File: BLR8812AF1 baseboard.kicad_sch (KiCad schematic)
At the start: 28 parts, among them U1 MP2307DN, U2 USBLC6-2SC6, U3 BL-R8812AF1, X1 TYPE-C-31-M-12

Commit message: Working on board
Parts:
- removed MH (x3): MountingHole, symbol Mechanical:MountingHole
- added MH2, MH3, MH4: MountingHole, MountingHole:MountingHole_2.2mm_M2, symbol Mechanical:MountingHole
- added X2, X5: ~, ULF:TH_1.7_1.7_1, symbol Ulf:TH_1_Pin
- added X3, X4, X6: ~, ULF:TH_1_1_0.65, symbol Ulf:TH_1_Pin
- C1, C2: value 10u -> 22u
- L1: footprint PCM_Inductor_SMD_AKL:L_7.3x7.3_H4.5 -> Inductor_SMD:L_SXN_SMDRI62
- MH1: renamed from MH; footprint (none) -> MountingHole:MountingHole_2.2mm_M2
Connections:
- net GND: now also X5.1 (Pin_1), X6.1 (Pin_1)
- net VBUS: now also X2.1 (Pin_1)
- net DP: now reaches U2.1 (I/O1), X1.A6 (DP1), X1.B6 (DP2)
- net DP: now also X3.1 (Pin_1)
- net DN: now reaches U2.3 (I/O2), X1.A7 (DN1), X1.B7 (DN2)
- net DN: now also X4.1 (Pin_1)
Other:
- moved on the sheet: C8, D1

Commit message: Completed placing
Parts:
- added D2: DNP, LED_SMD:LED_0603_1608Metric, symbol Device:LED
- added R10: DNP, Resistor_SMD:R_0402_1005Metric, symbol Device:R
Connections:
- net 3V3: now also R10.2
- net GND: now also D2.1 (K)
- net D1_P: now reaches R4.1, U2.6 (I/O1)
- net D2_P: now reaches R4.2, U3.4 (DP)
- net D2_N: now reaches R5.2, U3.3 (DN)
- net D1_N: now reaches R5.1, U2.4 (I/O2)
- new net: D2.2 (A), R10.1
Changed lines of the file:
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@@
 	)
 	(junction
+		(at 142.24 153.67)
+		(diameter 0)
+		(color 0 0 0 0)
+	)
+	(junction
 		(at 46.99 88.9)
 		(diameter 0)
@@
 	(wire
 		(pts
+			(xy 152.4 148.59) (xy 152.4 153.67)
+		)
+		(stroke
+			(width 0)
+			(type default)
+		)
+	)
+	(wire
+		(pts
 			(xy 132.08 69.85) (xy 129.54 69.85)
 		)
@@
 	(wire
 		(pts
+			(xy 152.4 132.08) (xy 152.4 127)
+		)
+		(stroke
+			(width 0)
+			(type default)
+		)
+	)
+	(wire
+		(pts
 			(xy 200.66 53.34) (xy 200.66 52.07)
 		)
@@
 	(wire
 		(pts
+			(xy 152.4 127) (xy 142.24 127)
+		)
+		(stroke
+			(width 0)
+			(type default)
+		)
+	)
+	(wire
+		(pts
 			(xy 142.24 124.46) (xy 142.24 127)
 		)
@@
 	(wire
 		(pts
+			(xy 152.4 139.7) (xy 152.4 140.97)
+		)
+		(stroke
+			(width 0)
+			(type default)
+		)
+	)
+	(wire
+		(pts
 			(xy 62.23 40.64) (xy 68.58 40.64)
 		)
@@
 	(wire
 		(pts
+			(xy 152.4 153.67) (xy 142.24 153.67)
+		)
+		(stroke
+			(width 0)
+			(type default)
+		)
+	)
+	(wire
+		(pts
 			(xy 43.18 143.51) (xy 49.53 143.51)
 		)
@@
 		)
 	)
+	(label "D2_P"
+		(at 106.68 38.1 0)
+		(fields_autoplaced yes)
+		(effects
+			(font
+				(size 1.27 1.27)
+			)
+			(justify left bottom)
+		)
+	)
+	(label "D2_N"
+		(at 106.68 40.64 0)
+		(fields_autoplaced yes)
+		(effects
+			(font
+				(size 1.27 1.27)
+			)
+			(justify left bottom)
+		)
+	)
 	(label "DP"
 		(at 177.8 57.15 180)
@@
 		)
 	)
+	(label "D1_P"
+		(at 88.9 38.1 0)
+		(fields_autoplaced yes)
+		(effects
+			(font
+				(size 1.27 1.27)
+			)
+			(justify left bottom)
+		)
+	)
 	(label "DN"
 		(at 72.39 40.64 0)
@@
 		)
 	)
+	(label "D1_N"
+		(at 88.9 40.64 0)
+		(fields_autoplaced yes)
+		(effects
+			(font
+				(size 1.27 1.27)
+			)
+			(justify left bottom)
+		)
+	)
 	(symbol
 		(lib_id "Mechanical:MountingHole")
@@
 	)
 	(symbol
+		(lib_id "Device:LED")
+		(at 152.4 144.78 90)
+		(unit 1)
+		(exclude_from_sim no)
+		(in_bom yes)
+		(on_board yes)
+		(dnp no)
+		(property "Reference" "D2"
+			(at 155.194 144.78 0)
+			(effects
+				(font
+					(size 1.27 1.27)
+				)
+			)
+		)
+		(property "Value" "DNP"
+			(at 149.86 144.78 0)
+			(effects
+				(font
+					(size 1.27 1.27)
+				)
+			)
+		)
+		(property "Footprint" "LED_SMD:LED_0603_1608Metric"
+			(at 152.4 144.78 0)
+			(effects
+				(font
+					(size 1.27 1.27)
+				)
+				(hide yes)
+			)
+		)
+		(property "Datasheet" "~"
+			(at 152.4 144.78 0)
+			(effects
+				(font
+					(size 1.27 1.27)
+				)
+				(hide yes)
+			)
+		)
+		(property "Description" "Light emitting diode"
+			(at 152.4 144.78 0)
+			(effects
+				(font
+					(size 1.27 1.27)
+				)
+				(hide yes)
+			)
+		)
+		(pin "2"
+		)
+		(pin "1"
+		)
+		(instances
+			(project "BLR8812AF1 baseboard"
+				(path "/eaa389b1-c28c-408b-8713-22e94bf6c980"
+					(reference "D2")
+					(unit 1)
+				)
+			)
+		)
+	)
+	(symbol
 		(lib_id "Device:R")
 		(at 99.06 148.59 180)
@@
 					(unit 1)
 				)
+			)
+		)
+	)
+	(symbol
+		(lib_id "Device:R")
+		(at 152.4 135.89 180)
+		(unit 1)
+		(exclude_from_sim no)
+		(in_bom yes)
+		(on_board yes)
+		(dnp no)
+		(property "Reference" "R10"
+			(at 150.114 135.89 90)
+			(effects
+				(font
+					(size 1.27 1.27)
+				)
+			)
+		)
+		(property "Value" "DNP"
+			(at 154.94 135.89 90)
+			(effects
+				(font
+					(size 1.27 1.27)
+				)
+			)
+		)
+		(property "Footprint" "Resistor_SMD:R_0402_1005Metric"
+			(at 154.178 135.89 90)
+			(effects
+				(font
+					(size 1.27 1.27)
+				)
+				(hide yes)
+			)
+		)
+		(property "Datasheet" "~"
+			(at 152.4 135.89 0)
+			(effects
+				(font
+					(size 1.27 1.27)
+				)
+				(hide yes)
+			)
+		)
+		(property "Description" "Resistor"
+			(at 152.4 135.89 0)
+			(effects
+				(font
+					(size 1.27 1.27)
+				)
+				(hide yes)
+			)
+		)
+		(pin "1"
+		)
+		(pin "2"
+		)
+		(instances
+			(project "BLR8812AF1 baseboard"
+				(path "/eaa389b1-c28c-408b-8713-22e94bf6c980"
+					(reference "R10")
+					(unit 1)
+				)

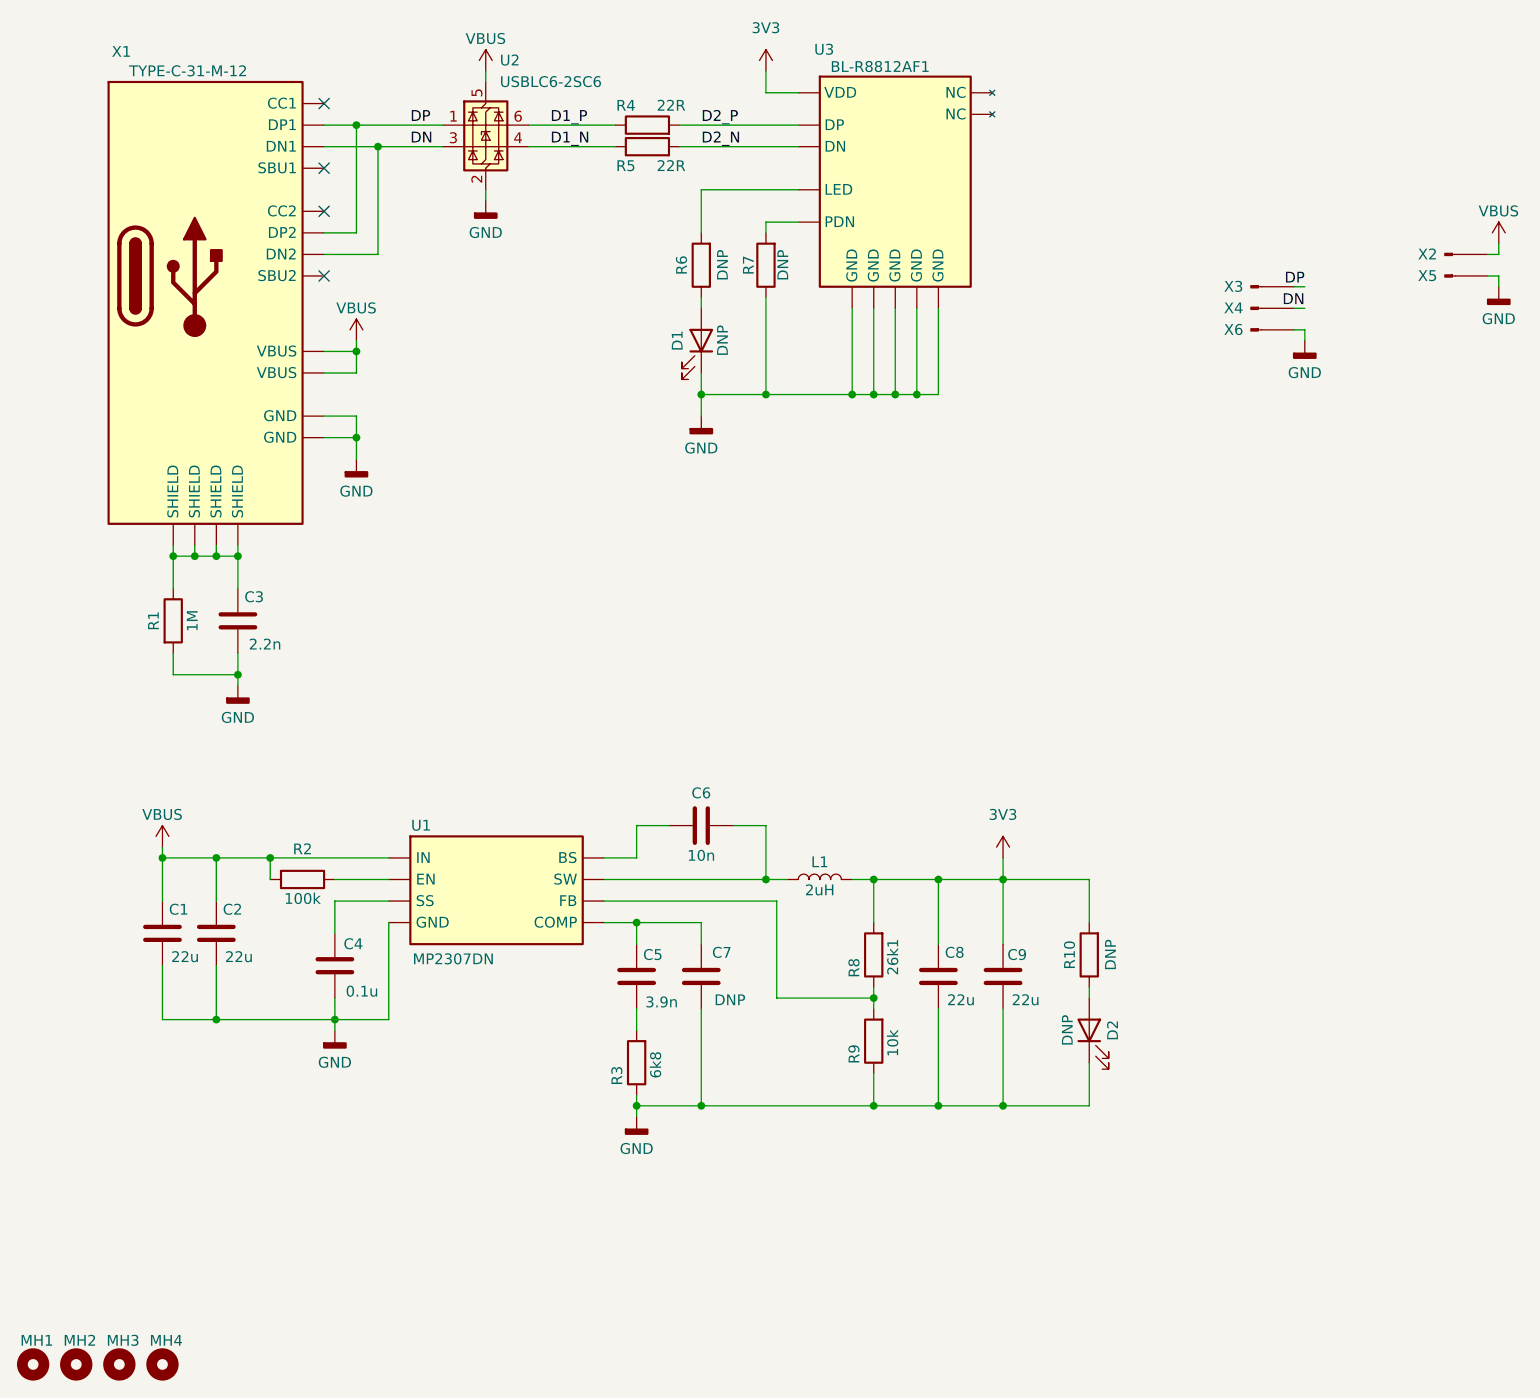
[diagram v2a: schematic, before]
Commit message: changed DC-DC
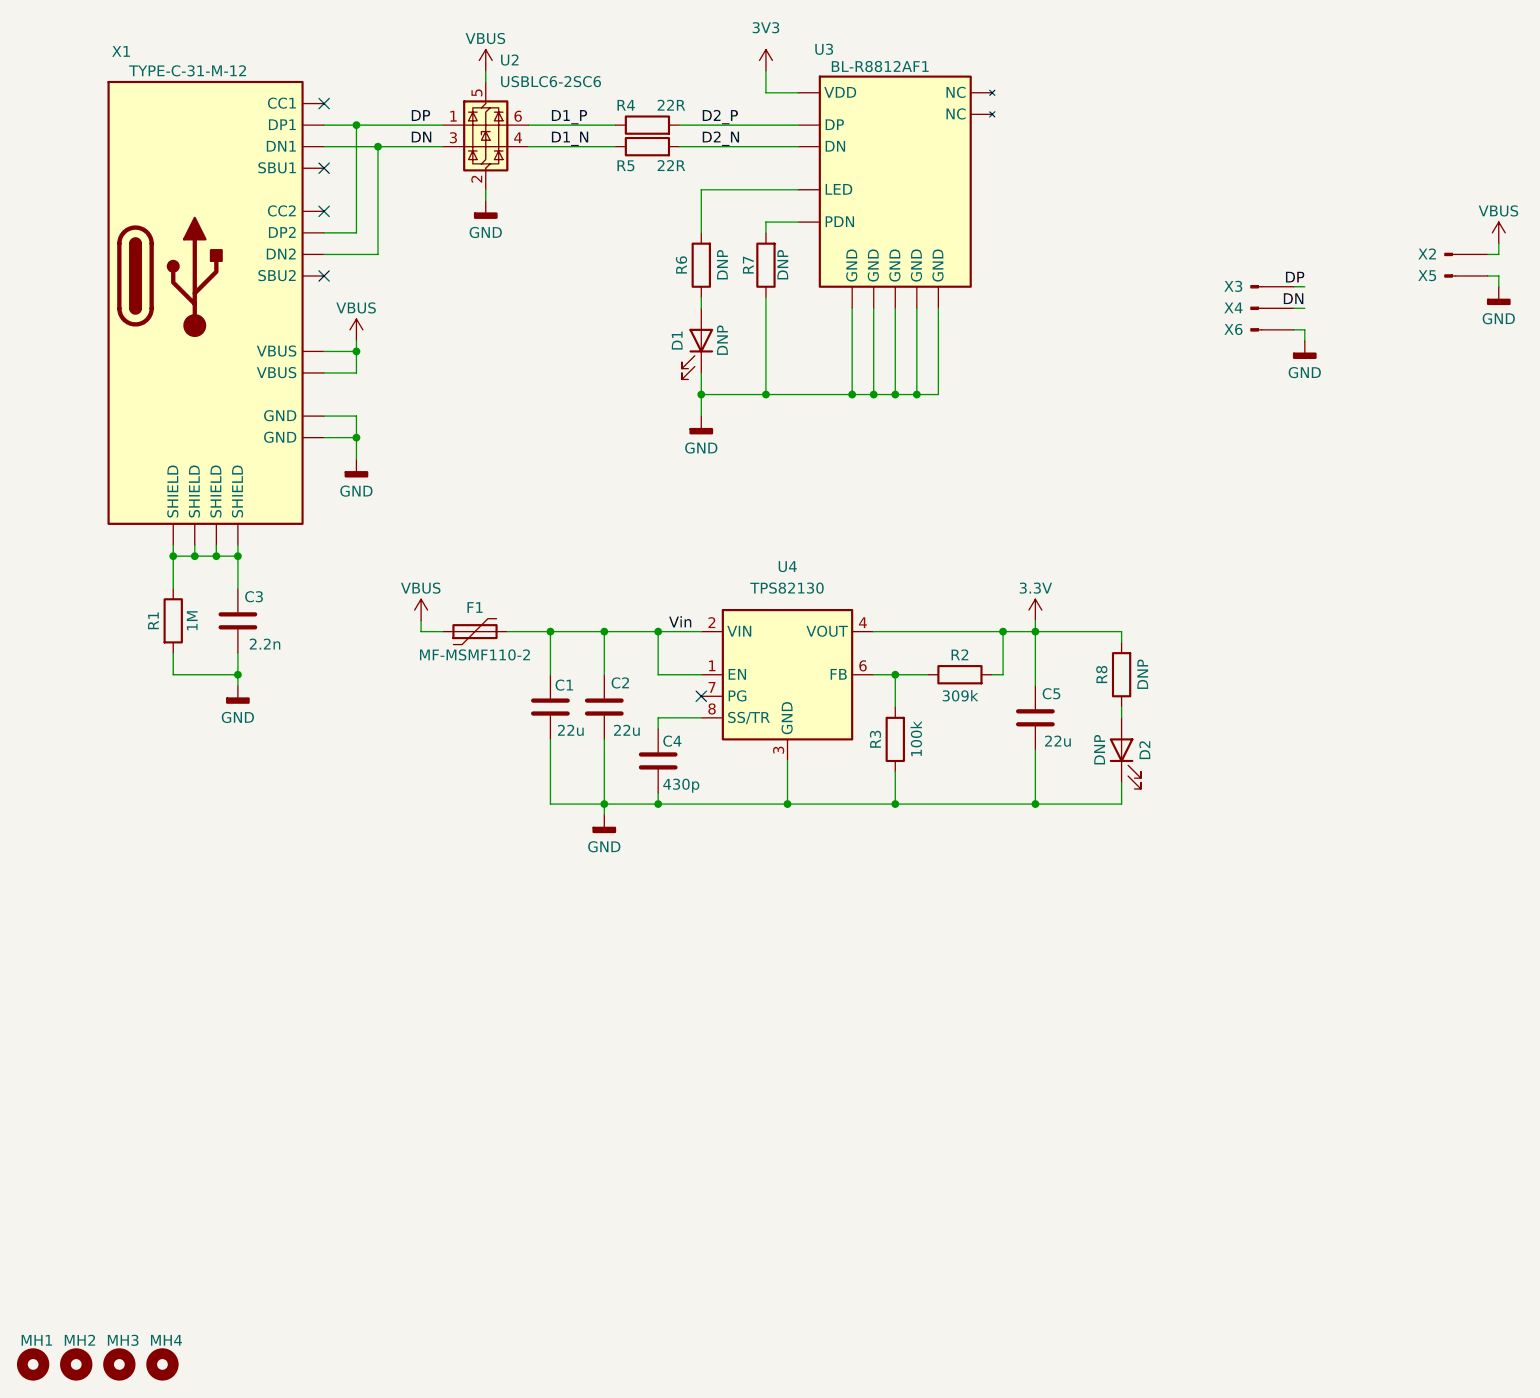
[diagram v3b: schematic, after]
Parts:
- removed C6: 10n, Capacitor_SMD:C_0402_1005Metric, symbol Device:C
- removed C7: DNP, Capacitor_SMD:C_0402_1005Metric, symbol Device:C
- removed C8, C9: 22u, Capacitor_SMD:C_1206_3216Metric, symbol Device:C
- removed L1: 2uH, Inductor_SMD:L_SXN_SMDRI62, symbol Device:L
- removed R10: DNP, Resistor_SMD:R_0402_1005Metric, symbol Device:R
- removed R9: 10k, Resistor_SMD:R_0402_1005Metric, symbol Device:R
- removed U1: MP2307DN, Package_SO:SOIC-8-1EP_3.9x4.9mm_P1.27mm_EP2.62x3.51mm, symbol Ulf:MP2307DN
- added F1: MF-MSMF110-2, Fuse:Fuse_1812_4532Metric_Pad1.30x3.40mm_HandSolder, symbol Device:Polyfuse
- added U4: TPS82130, Package_LGA:Texas_SIL0008D_MicroSiP-8-1EP_2.8x3mm_P0.65mm_EP1.1x1.9mm_ThermalVias, symbol Regulator_Switching:TPS82130
- C4: value 0.1u -> 430p
- C5: value 3.9n -> 22u; footprint Capacitor_SMD:C_0402_1005Metric -> Capacitor_SMD:C_1206_3216Metric
- R2: value 100k -> 309k
- R3: value 6k8 -> 100k
- R8: value 26k1 -> DNP
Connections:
- net 3V3: no longer R8.2
- net GND: now also C5.2, U4.3 (GND), U4.9 (GND)
- net VBUS: now also F1.1; no longer C1.1, C2.1, R2.2
- net at D2.2 (A): now also R8.1
- net at R3.2: now also R2.1, U4.6 (FB); no longer C5.2
- net 3.3V: now reaches C5.1
- net 3.3V: now also R2.2, R8.2, U4.4 (VOUT), U4.5 (VOUT)
- net at C4.1: now also U4.8 (SS/TR)
- new net Vin: C1.1, C2.1, F1.2, U4.1 (EN), U4.2 (VIN)
- no-connect marks 4 -> 5
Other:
- moved on the sheet: C1, C2

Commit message: almost done
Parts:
- removed C3: 2.2n, Capacitor_SMD:C_1206_3216Metric, symbol Device:C
- added C5: 22u, Capacitor_SMD:C_1206_3216Metric, symbol Device:C
- added Q1: AO3401A, Package_TO_SOT_SMD:SOT-23, symbol Transistor_FET:AO3401A
- R1: value 1M -> 10k; footprint Resistor_SMD:R_1206_3216Metric -> Resistor_SMD:R_0402_1005Metric
- renumbered C4 to C3, C5 to C4, R4 to R2, R5 to R3, R6 to R4, R7 to R5, R3 to R6, R2 to R7, U2 to U1, U3 to U2, U4 to U3, X3 to X2, X4 to X3, X6 to X4, X2 to X5, X5 to X6
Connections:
- net 3V3 is gone; now on net +3.3V: U2.2 (VDD)
- net GND: now also R1.1, X1.SHIELD, C5.2; no longer R1.2
- net Vin: now also Q1.3 (D); no longer F1.2
- net 3.3V renamed +3.3V
- net +3.3V: now also C5.1
- net VBUS renamed +VBUS
- new net: F1.2, Q1.2 (S)
- new net: Q1.1 (G), R1.2
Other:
- moved on the sheet: C1, C2, C3, C4, D1, D2, F1, R4, R5, R6, R7, R8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
